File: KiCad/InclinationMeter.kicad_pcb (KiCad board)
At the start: 4 copper layers, 130 x 35 mm, 102 parts, among them J1 JST_PH_2.0mm_1x02, J3 Header_FFC_1.0mm_06, J4 Header_50mil_2x07, J5 Header_FFC_1.0mm_10, J6 Header_FFC_1.0mm_10, Q1 DMG2305UX, Q2 FS8205A, Q3 AO3400A, Q4 AO3400A, SW1 PEC11R-4215F-S0024, SW2 PEC11R-4215F-S0024, U1 DW01A, U10 SN74HC14PWR, U11 LM35DGS, U2 LP5907MFX-3.3/NOPB, U3 TP4056, U4 LP5907MFX-3.3/NOPB, U5 SD6210A, U6 STM32G0B1RET6, U7 RN4871-I_RM128, U8 SN74AHCT244DBR, U9 24LC256-I_ST, Y1 32.768kHz, Y2 8MHz

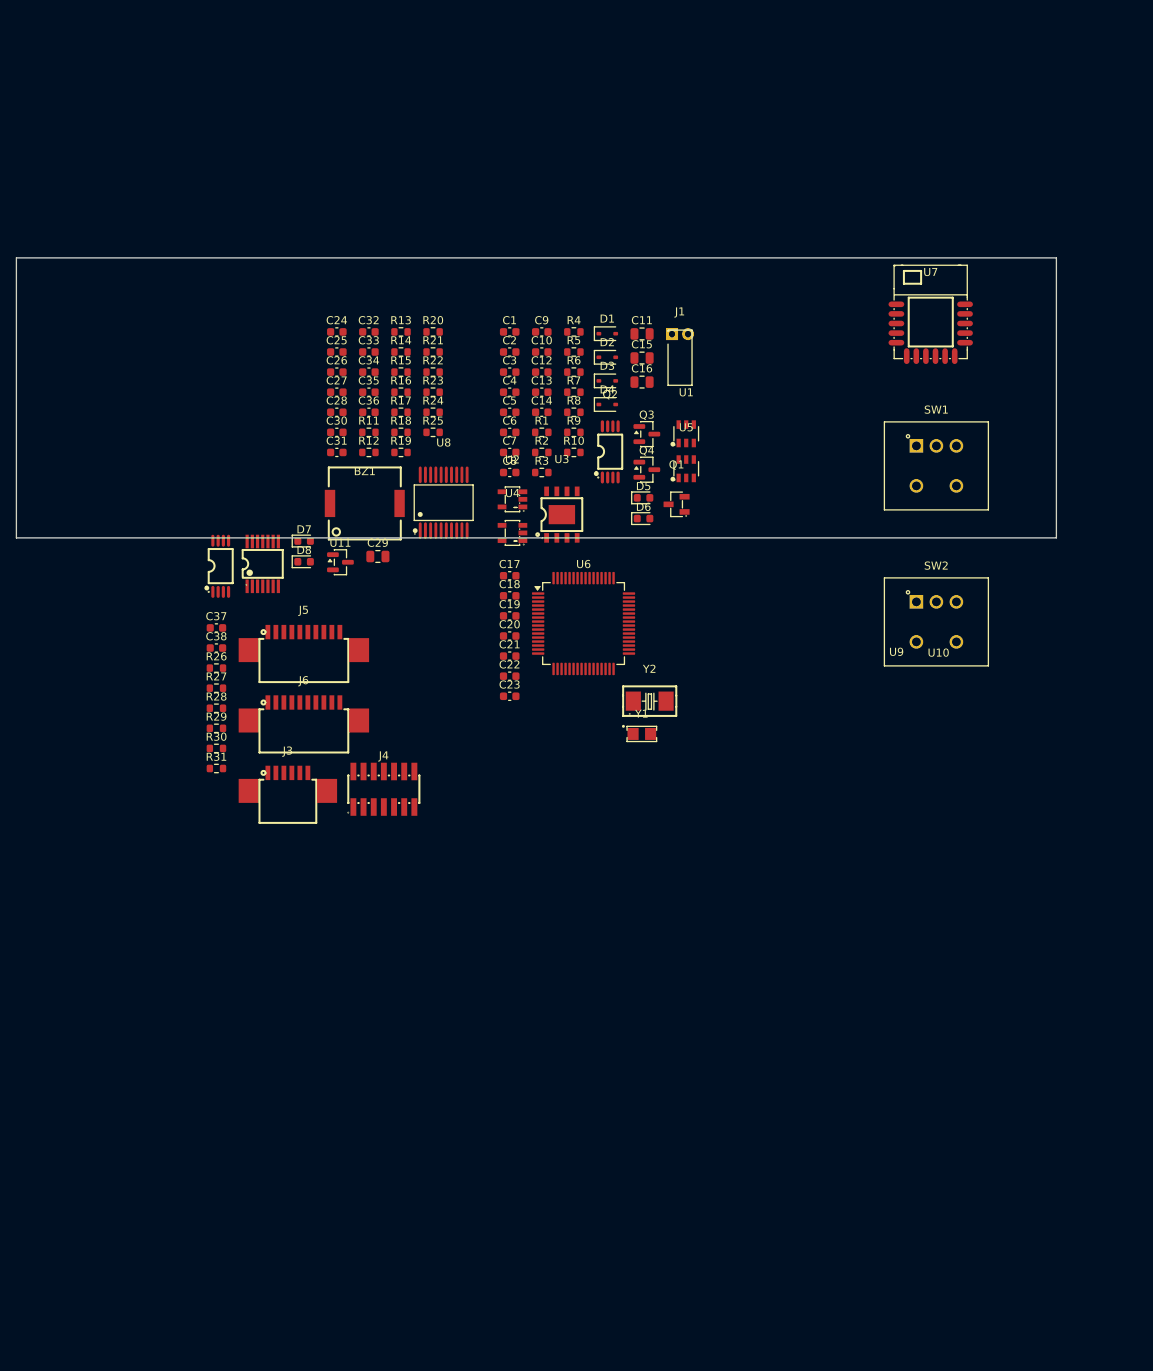
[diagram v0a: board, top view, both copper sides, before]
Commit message: Restore manual KiCad edits lost in 2026-05-10 force-push reset
Recovers connectors/mcu/power/ui schematics and the PCB layout from the
manual saves captured in KiCad/.history/ (timestamp 2026-05-10 19:55),
which were wiped when the working tree was hard-reset to origin/master
after an amended Schematic finalized force-push.

Co-Authored-By: Claude Opus 4.7 <noreply@anthropic.com>
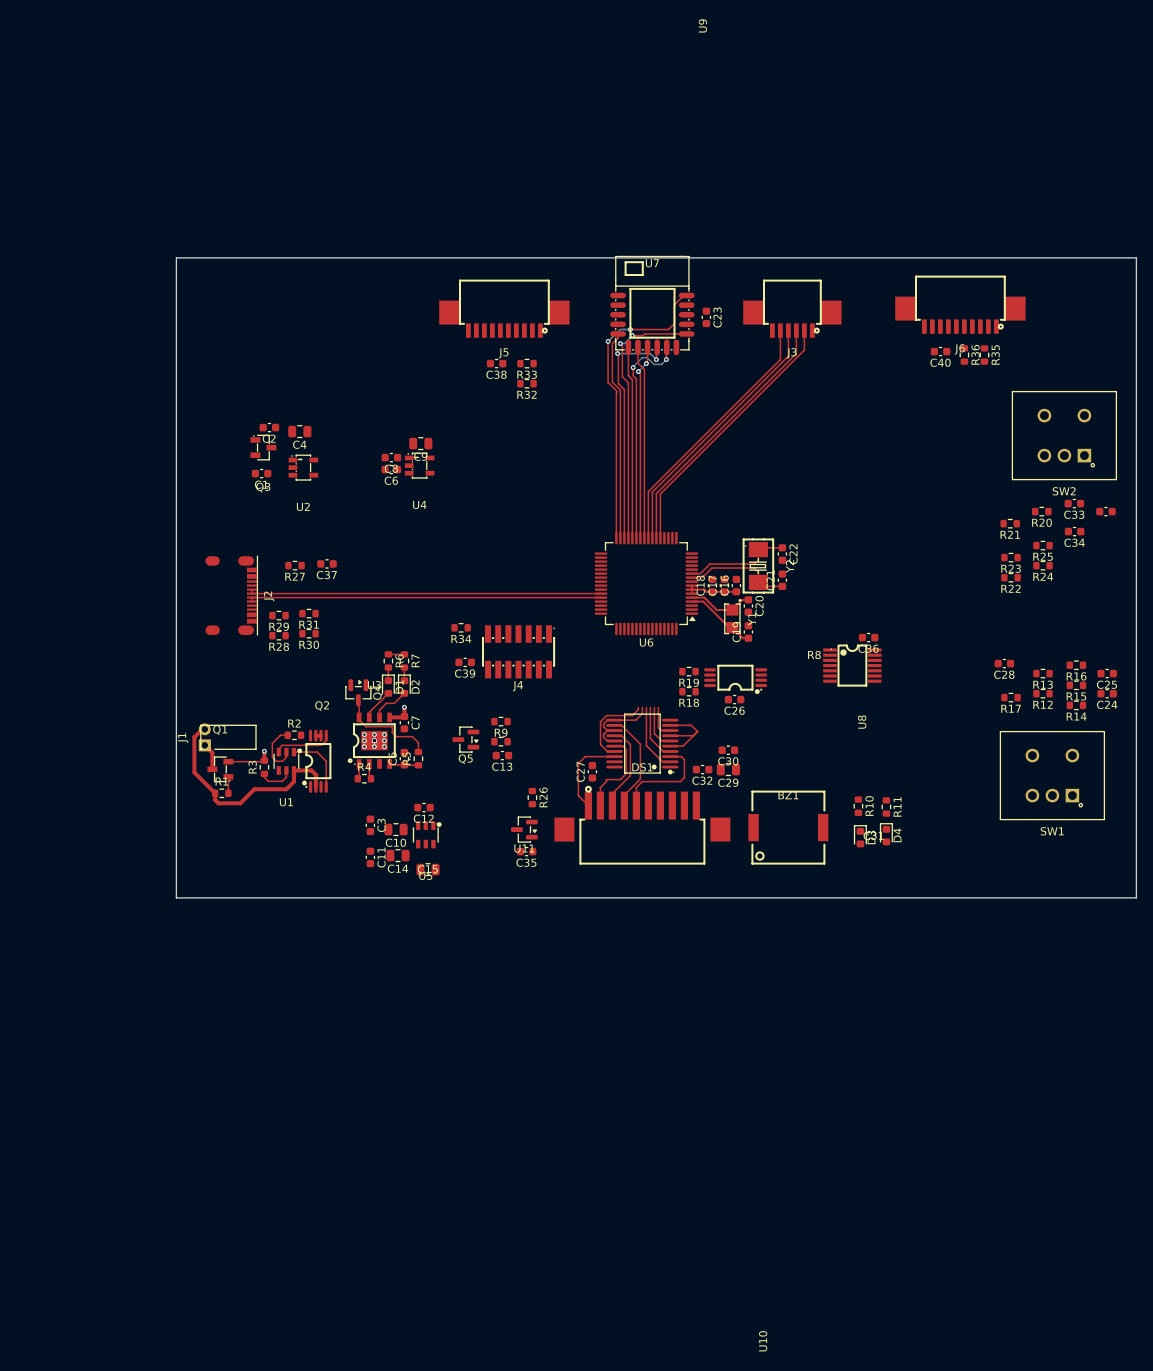
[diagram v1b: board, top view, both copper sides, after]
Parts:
- removed the C1 at (86.7, 34.3)
- removed the C10 at (90.7, 36.8)
- removed the C5 at (86.7, 44.3)
- removed the D1 at (98.9, 34.5)
- removed the D2 at (98.9, 37.4)
- removed the D3 at (98.9, 40.4)
- removed the D4 at (98.9, 43.3)
- removed the R2 at (90.7, 49.3)
- added C18: 100n, sldrnrd:C_0603, F.Cu at (112.0, 66.0)
- added C38: 100n, sldrnrd:C_0603, F.Cu at (85.0, 38.2)
- added C4: 10u, sldrnrd:C_0805, F.Cu at (60.4, 46.7)
- added C40: 100n, sldrnrd:C_0603, F.Cu at (140.5, 36.7)
- added C9: 10u, sldrnrd:C_0805, F.Cu at (75.5, 48.2)
- added DS1: LS027B7DH01, sldrnrd:Header_FFC_1.5mm_10, F.Cu at (103.2, 95.2)
- added J2: USB-C, sldrnrd:USB_C, F.Cu at (52.0, 67.2)
- added Q3: DMG2305UX, sldrnrd:SOT-23-BR, F.Cu at (55.9, 48.7)
- added R18: 5k1, sldrnrd:R_0603, F.Cu at (109.1, 79.2)
- added R19: 5k1, sldrnrd:R_0603, F.Cu at (109.1, 76.7)
- added R32: 5k1, sldrnrd:R_0603, F.Cu at (88.8, 40.7)
- added R33: 5k1, sldrnrd:R_0603, F.Cu at (88.8, 38.2)
- added R35: 5k1, sldrnrd:R_0603, F.Cu at (146.0, 37.1)
- added R36: 5k1, sldrnrd:R_0603, F.Cu at (143.5, 37.1)
- moved C24 106.4 mm to (161.3, 79.5), turned to 180 degrees
- moved C25 104.3 mm to (161.3, 77.0), turned to 180 degrees
- moved C31 96.4 mm to (161.2, 56.7), turned to 180 degrees
- moved J6 96.4 mm to (143.0, 31.8), turned to 180 degrees
- moved R14 94.1 mm to (157.5, 80.9), turned to 180 degrees
- moved R12 92.1 mm to (153.3, 79.5), turned to 180 degrees
- moved R15 92.0 mm to (157.5, 78.4), turned to 180 degrees
- moved C34 90.4 mm to (157.3, 59.2), turned to 180 degrees
- moved C33 90.2 mm to (157.2, 55.7), turned to 180 degrees
- moved R16 90.2 mm to (157.5, 75.9), turned to 180 degrees
- moved R13 89.8 mm to (153.3, 77.0), turned to 180 degrees
- moved C28 89.2 mm to (148.5, 75.7), turned to 180 degrees
- moved J3 86.2 mm to (122.0, 32.3), turned to 180 degrees
- moved R17 83.1 mm to (149.3, 80.0), turned to 180 degrees
- moved R20 80.4 mm to (153.2, 56.7), turned to 180 degrees
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- renumbered C2 to C1, C11 to C10, C12 to C11, C13 to C12, C14 to C13, C15 to C14, C16 to C15, C17 to C16, C18 to C17, C4 to C2, C38 to C39, C6 to C5, C7 to C6, C8 to C7, C9 to C8, D5 to D1, D6 to D2, D7 to D3, D8 to D4, Q3 to Q4, Q4 to Q5, R11 to R10, R12 to R11, R13 to R12, R14 to R13, R15 to R14, R16 to R15, R17 to R16, R18 to R17, R3 to R2, R19 to R20, R20 to R21, R21 to R22, R22 to R23, R23 to R24, R24 to R25, R25 to R26, R26 to R27, R27 to R28, R28 to R29, R4 to R3, R29 to R30, R30 to R31, R31 to R34, R5 to R4, R6 to R5, R7 to R6, R8 to R7, R9 to R8, R10 to R9
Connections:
- net ENC_1SW_RAW renamed ~{ENC_1SW_RAW}
- C16 pad 1: VCC -> 3V3_STANDBY
- C17 pad 1: VCC -> 3V3_STANDBY
- C2 pad 1: 3V3 -> 3V3_STANDBY
- C23 pad 1: VCC -> 3V3
- C36 pad 1: 3V3 -> 3V3_STANDBY
- J5 pad 4: 3V3 -> 3V3_Sensors
- J5 pad 6: 3V3 -> 3V3_Sensors
- J6 pad 4: 3V3 -> 3V3_Sensors
- J6 pad 6: 3V3 -> 3V3_Sensors
- R16 pad 1: PWR_ON -> 3V3_STANDBY
- R16 pad 2: GND -> Net-(SW1-SW1)
- R17 pad 1: PWR_ON -> Net-(SW1-SW1)
- R24 pad 1: 3V3 -> 3V3_STANDBY
- R24 pad 2: Net-(SW2-SW2) -> Net-(SW2-SW1)
- R25 pad 1: Net-(SW2-SW2) -> Net-(SW2-SW1)
- SW1 pad 4: VCC -> Net-(SW1-SW1)
- SW1 pad 5: PWR_ON -> GND
- SW2 pad 4: GND -> Net-(SW2-SW1)
- SW2 pad 5: Net-(SW2-SW2) -> GND
- U10 pad 14: 3V3 -> 3V3_STANDBY
- U10 pad 6: ~{ENC_1SW} -> ENC_1SW
- U2 pad 3: LDO_EN -> VCC
- U2 pad 5: 3V3 -> 3V3_STANDBY
- U4 pad 3: LDO_EN -> 3V3
- U6 pad 17: PCAP04_2_INT -> unconnected-(U6-PA0-Pad17)
- U6 pad 18: 3V3_EN -> PCAP04_2_INT
- U6 pad 19: 5V_EN -> VBUS_SENSE
- U6 pad 38: unconnected-(U6-PC6-Pad38) ->  ~{3v3_EN}
- U6 pad 39: unconnected-(U6-PC7-Pad39) -> 5V_EN
- U6 pad 42: VBUS_SENSE -> unconnected-(U6-PA10-Pad42)
- U6 pad 58: LED_PWR -> LED_STATUS
- U6 pad 59: LED_STATUS -> ENC_1SW
- U6 pad 6: unconnected-(U6-VBAT-Pad6) -> 3V3_STANDBY
- U6 pad 64: ~{ENC_1SW} -> LED_PWR
- U6 pad 7: GND -> 3V3_STANDBY
- U6 pad 8: VCC -> 3V3_STANDBY
- U7 pad 14: VCC -> 3V3
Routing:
- net USB_D-: track 0.00 -> 44.1 mm
- net USB_D+: track 0.00 -> 44.1 mm
- net BLE_P2_0: track 0.00 -> 38.7 mm, vias 0 -> 2
- net BLE_P0_2: track 0.00 -> 33.5 mm, vias 0 -> 2
- net SCL3300_CS: track 0.00 -> 33.4 mm
- net SCL3300_SCK: track 0.00 -> 33.2 mm
- net SCL3300_MISO: track 0.00 -> 33.0 mm
- net SCL3300_MOSI: track 0.00 -> 32.8 mm
- net BLE_P3_6: track 0.00 -> 30.2 mm, vias 0 -> 2
- net VCC: track 0.00 -> 28.5 mm, vias 0 -> 2
- net ~{BLE_RST}: track 0.00 -> 28.4 mm, vias 0 -> 2
- net BAT-: track 0.00 -> 27.7 mm
- net BLE_P1_7: track 0.00 -> 26.2 mm
- net BLE_UART_BLE_TO_MCU: track 0.00 -> 24.4 mm, vias 0 -> 2
- net BLE_UART_MCU_TO_BLE: track 0.00 -> 24.2 mm
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- added copper zone on In1.Cu, net GND
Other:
- board size 130 x 35 mm -> 120 x 80 mm
